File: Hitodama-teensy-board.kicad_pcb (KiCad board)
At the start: 2 copper layers, 119 x 174 mm, 16 parts, among them U4 Teensy3.6

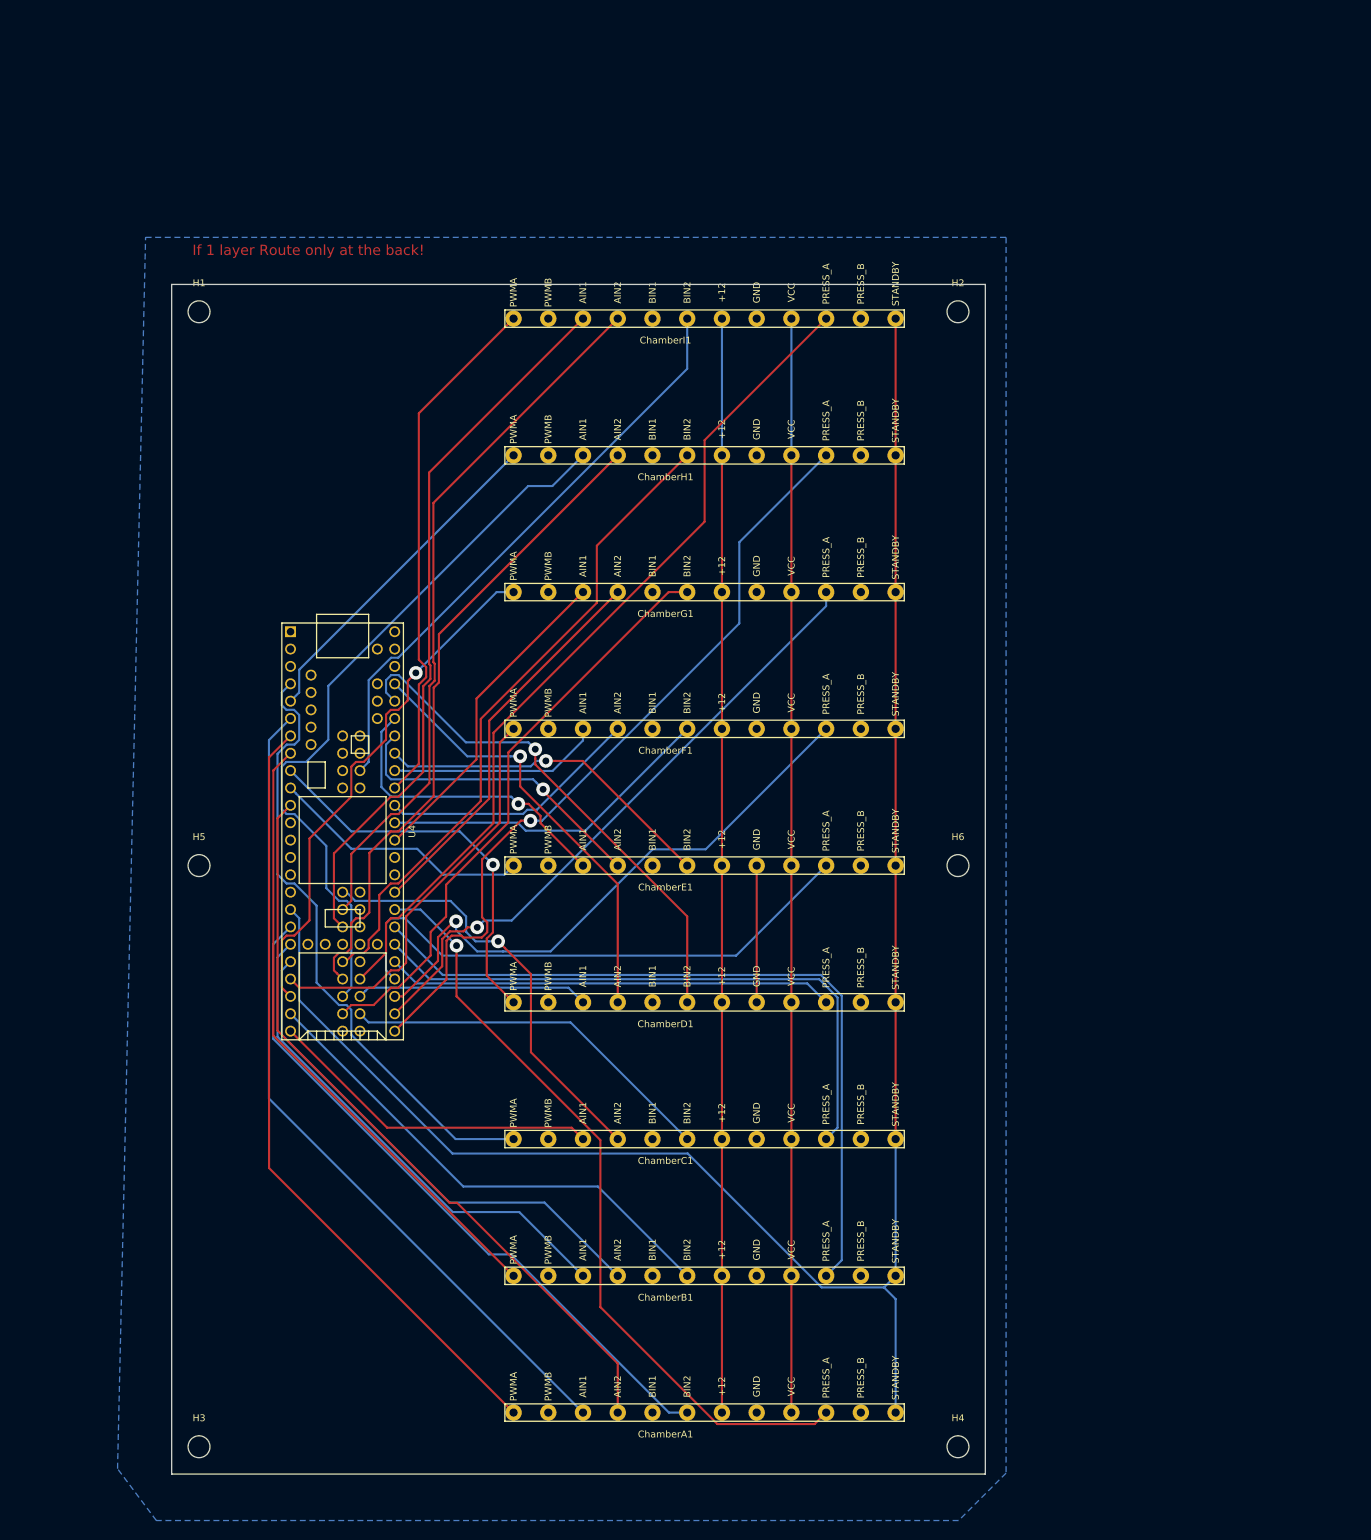
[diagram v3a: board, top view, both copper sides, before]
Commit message: schematic add SPI ports & 12 v power connector
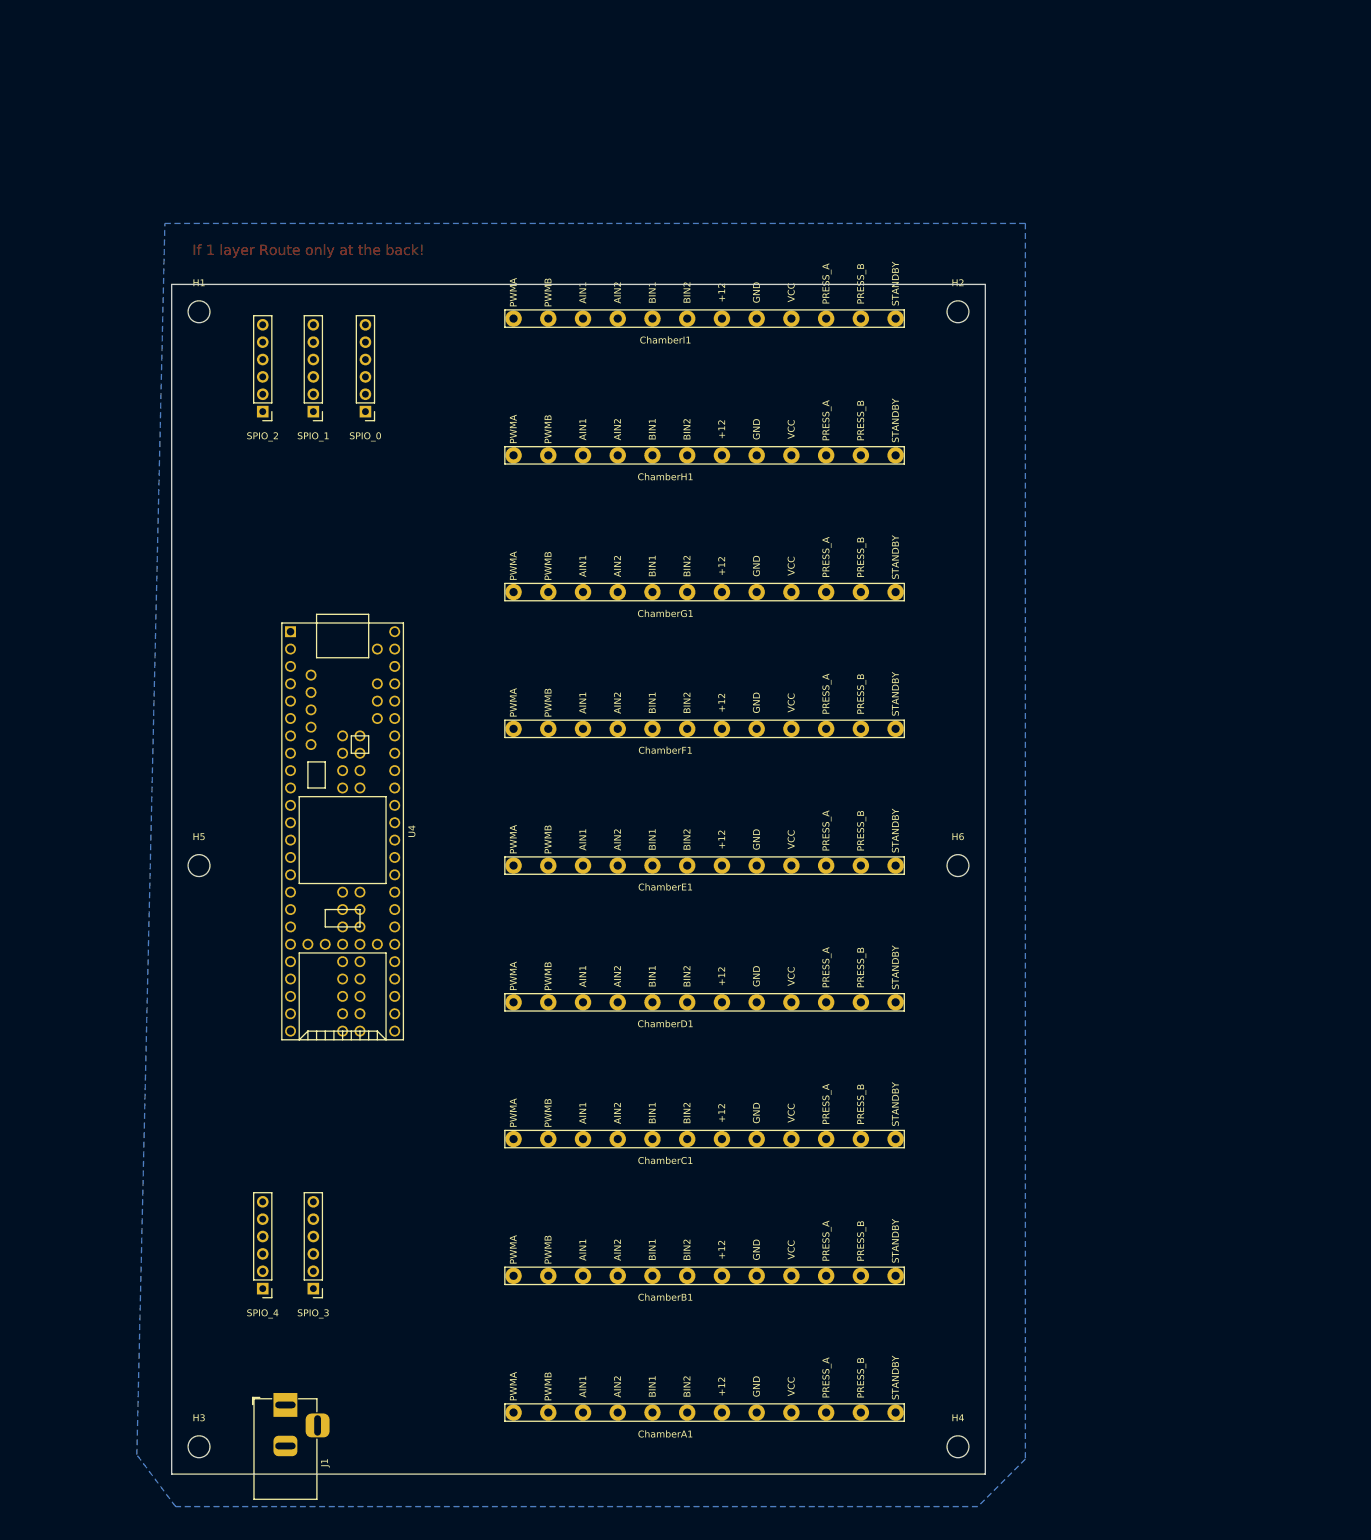
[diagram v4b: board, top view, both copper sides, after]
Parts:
- added J1: Jack-DC, Connector_BarrelJack:BarrelJack_Horizontal, F.Cu at (26.6, 173.9)
- added SPIO_0: Conn_01x06_Female, Connector_PinHeader_2.54mm:PinHeader_1x06_P2.54mm_Vertical, F.Cu at (38.3, 28.6)
- added SPIO_1: Conn_01x06_Female, Connector_PinHeader_2.54mm:PinHeader_1x06_P2.54mm_Vertical, F.Cu at (30.7, 28.6)
- added SPIO_2: Conn_01x06_Female, Connector_PinHeader_2.54mm:PinHeader_1x06_P2.54mm_Vertical, F.Cu at (23.3, 28.6)
- added SPIO_3: Conn_01x06_Female, Connector_PinHeader_2.54mm:PinHeader_1x06_P2.54mm_Vertical, F.Cu at (30.7, 156.9)
- added SPIO_4: Conn_01x06_Female, Connector_PinHeader_2.54mm:PinHeader_1x06_P2.54mm_Vertical, F.Cu at (23.3, 156.9)
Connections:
- U4 pad 80: /D51 -> /SPI0.CS4
- U4 pad 81: /D52 -> /SPI0.CS3
- U4 pad 82: /D53 -> /SPI0.CS2
- U4 pad 83: /D54 -> /SPI0.CS1
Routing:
- net /All.Stby: track 278.1 -> 0.00 mm
- net VCC: track 160.0 -> 0.00 mm
- net +12V: track 160.0 -> 0.00 mm
- net /ChamberI.ADC: track 125.4 -> 0.00 mm
- net /ChamberA.D1: track 121.8 -> 0.00 mm
- net /ChamberH.ADC: track 115.8 -> 0.00 mm, vias 1 -> 0
- net /ChamberA.PWM: track 115.1 -> 0.00 mm
- net /ChamberA.ADC: track 113.6 -> 0.00 mm, vias 1 -> 0
- net /ChamberB.ADC: track 111.5 -> 0.00 mm
- net /ChamberA.D2: track 110.8 -> 0.00 mm
- net /ChamberH.D1: track 107.2 -> 0.00 mm
- net /ChamberI.D1: track 105.4 -> 0.00 mm
- net /ChamberI.D2: track 103.9 -> 0.00 mm
- net /ChamberA.D3: track 100.6 -> 0.00 mm
- net /ChamberH.D3: track 96.7 -> 0.00 mm
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
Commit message: route & DRC teensy board
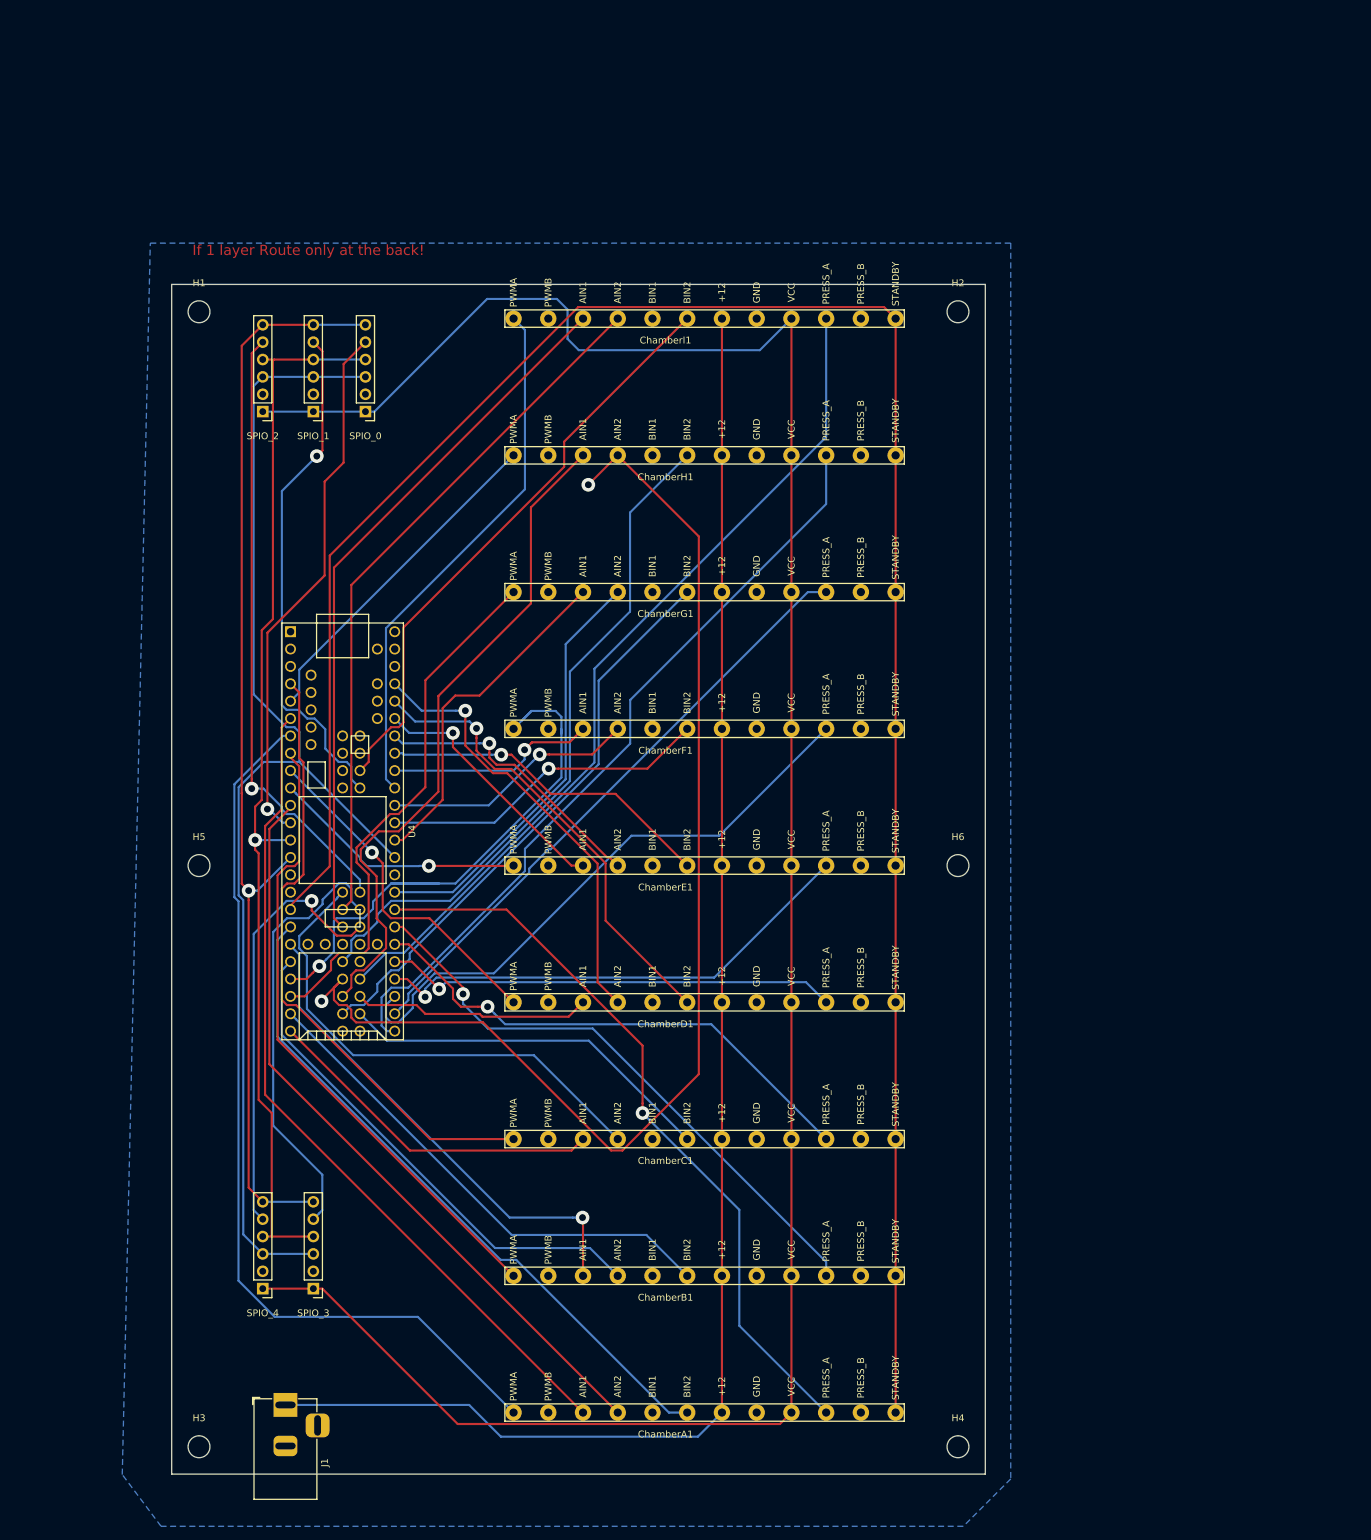
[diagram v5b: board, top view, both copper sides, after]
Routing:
- net VCC: track 0.00 -> 337.9 mm
- net /All.Stby: track 0.00 -> 312.7 mm
- net +12V: track 0.00 -> 227.2 mm
- net /SPI0.SCK: track 0.00 -> 182.6 mm
- net /ChamberH.D2: track 0.00 -> 177.4 mm, vias 0 -> 2
- net /SPI0.MISO: track 0.00 -> 161.4 mm, vias 0 -> 1
- net /SPI0.MOSI: track 0.00 -> 157.9 mm, vias 0 -> 1
- net /ChamberA.PWM: track 0.00 -> 132.2 mm
- net /ChamberI.ADC: track 0.00 -> 126.4 mm
- net /ChamberA.D1: track 0.00 -> 122.3 mm
- net /ChamberH.ADC: track 0.00 -> 114.1 mm
- net /ChamberA.D2: track 0.00 -> 111.2 mm
- net /ChamberA.ADC: track 0.00 -> 109.3 mm, vias 0 -> 1
- net /ChamberI.D1: track 0.00 -> 104.6 mm
- net /ChamberI.D2: track 0.00 -> 103.1 mm
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
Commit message: separated the teensy board into four modules, so that it fits in smaller PCB's. Improved the chamber board, and added rules so that auto-router can figure out the optimal 1 layer+jumpers route
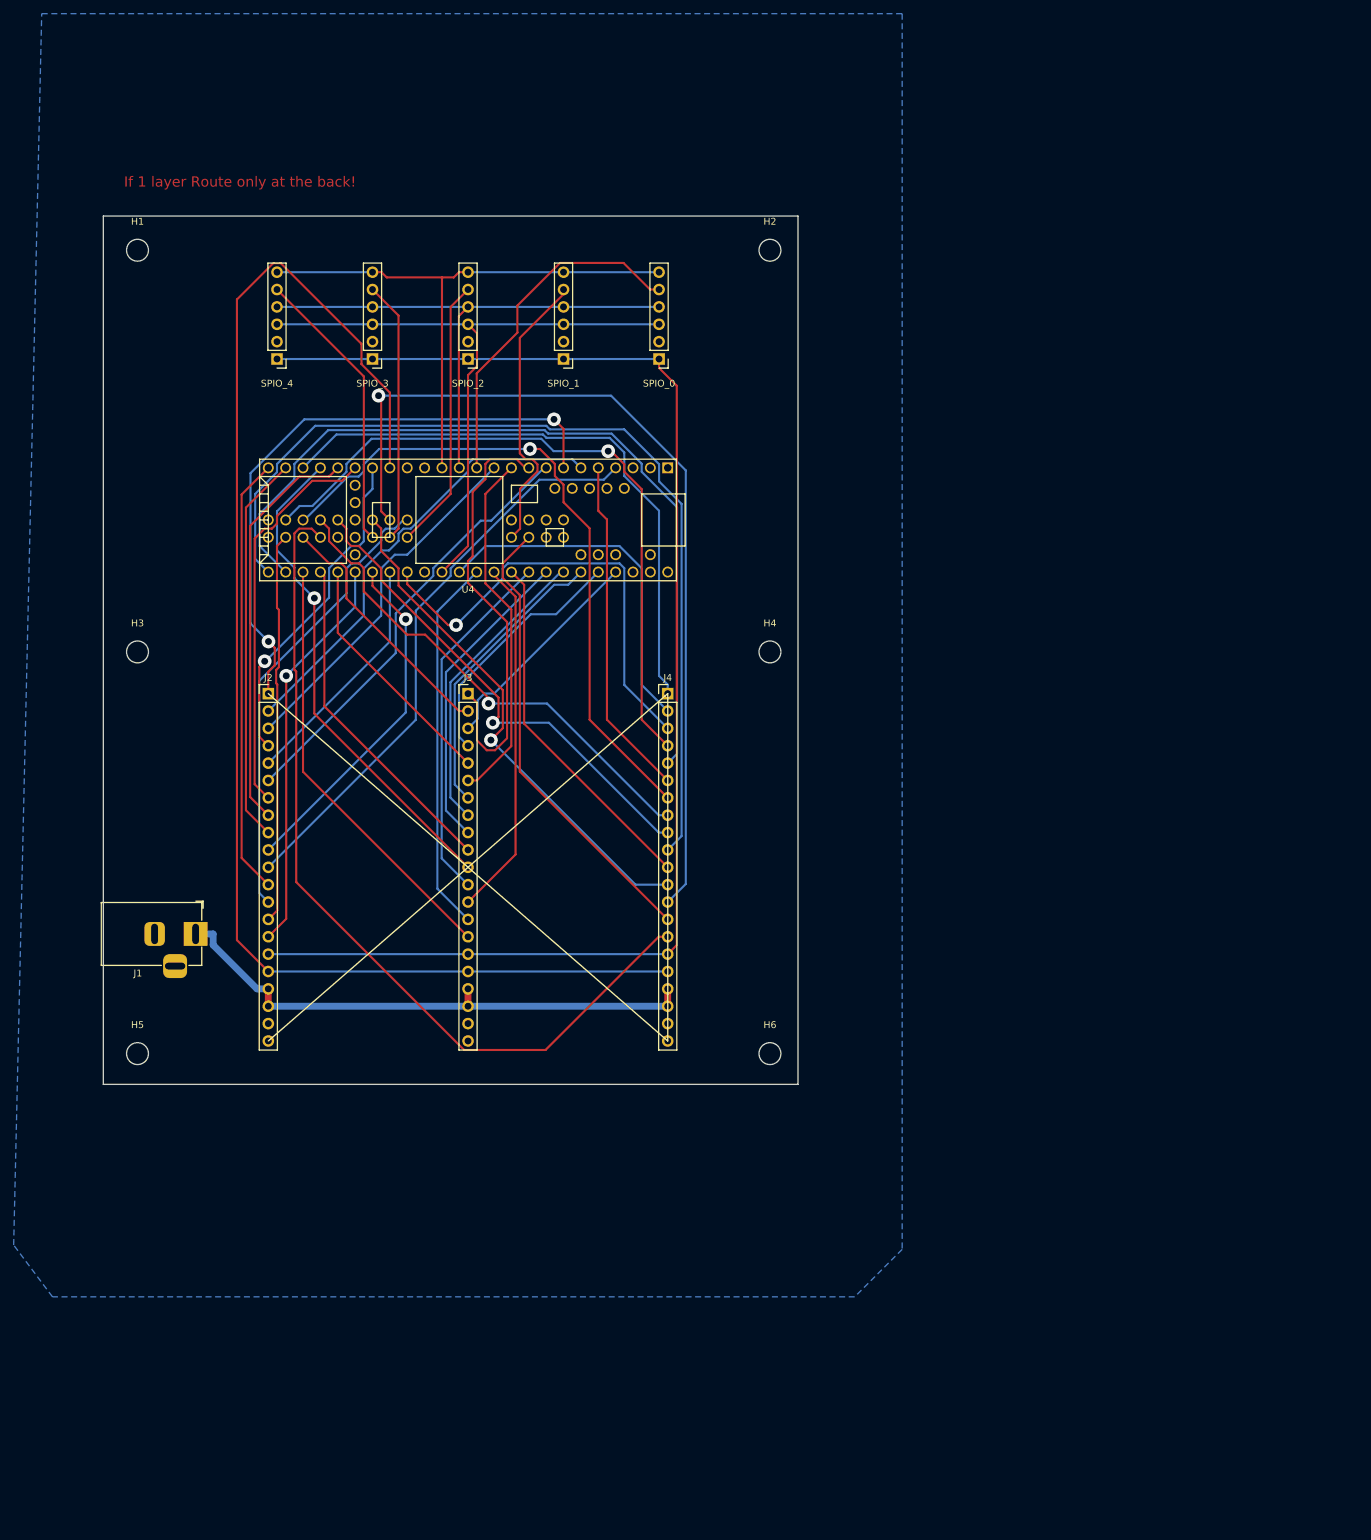
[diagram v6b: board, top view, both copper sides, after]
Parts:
- removed ChamberA1, ChamberB1, ChamberC1, ChamberD1, ChamberE1, ChamberF1, ChamberG1, ChamberH1, ChamberI1: ChamberBoard_Holder, chamber_board_holder:chamber_board_holder
- added J2: Conn_01x21_Female, Connector_PinHeader_2.54mm:PinHeader_1x21_P2.54mm_Vertical, F.Cu at (24.1, 69.8)
- added J3: Conn_01x21_Female, Connector_PinHeader_2.54mm:PinHeader_1x21_P2.54mm_Vertical, F.Cu at (53.3, 69.8)
- added J4: Conn_01x21_Female, Connector_PinHeader_2.54mm:PinHeader_1x21_P2.54mm_Vertical, F.Cu at (82.5, 69.8)
- moved SPIO_3 136.2 mm to (39.4, 20.9)
- moved SPIO_4 136.0 mm to (25.4, 20.9)
- moved H4 119.5 mm to (97.5, 63.8)
- moved H3 116.6 mm to (5.00, 63.8)
- moved J1 70.1 mm to (13.5, 105.0), turned to 0 degrees
- moved U4 49.1 mm to (53.3, 44.5), turned to 180 degrees
- moved SPIO_0 43.6 mm to (81.3, 20.9)
- moved H6 38.9 mm to (97.5, 122.5)
- moved SPIO_1 37.4 mm to (67.3, 20.9)
- moved SPIO_2 31.0 mm to (53.3, 20.9)
- moved H2 28.9 mm to (97.5, 5.00)
- moved H5 28.9 mm to (5.00, 122.5)
- moved H1 12.7 mm to (5.00, 5.00)
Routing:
- net +12V: track 227.2 -> 80.9 mm
- net VCC: track 337.9 -> 203.0 mm
- net /All.Stby: track 312.7 -> 203.8 mm
- net /ChamberH.D2: track 177.4 -> 72.2 mm, vias 2 -> 1
- net /SPI0.SCK: track 182.6 -> 94.8 mm
- net /SPI0.MOSI: track 157.9 -> 80.0 mm, vias 1 -> 0
- net /SPI0.MISO: track 161.4 -> 84.4 mm, vias 1 -> 0
- net /ChamberA.ADC: track 109.3 -> 35.3 mm, vias 1 -> 0
- net /ChamberA.D2: track 111.2 -> 52.8 mm
- net /ChamberA.D1: track 122.3 -> 66.8 mm
- net /ChamberA.D3: track 99.5 -> 48.8 mm, vias 0 -> 1
- net /SPI0.CS2: track 89.3 -> 39.9 mm, vias 1 -> 0
- net /ChamberA.PWM: track 132.2 -> 89.4 mm, vias 0 -> 2
- net /ChamberB.ADC: track 86.8 -> 51.0 mm
- net /SPI0.CS1: track 75.3 -> 42.1 mm, vias 1 -> 0
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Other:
- board size 119 x 174 mm -> 101.6 x 127 mm
- net class Power added: clearance 0.31, trace_width 1, via_dia 2, via_drill 1

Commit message: teensy board change 21 pins headers into 20 pins headers.
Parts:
- J2, J3, J4: value Conn_01x21_Female -> Conn_01x20_Female; footprint Connector_PinHeader_2.54mm:PinHeader_1x21_P2.54mm_Vertical -> Connector_PinHeader_2.54mm:PinHeader_1x20_P2.54mm_Vertical
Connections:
- J2 pad 19: +12V -> GND
- J2 pad 20: GND -> Net-(J2-Pad20)
- J3 pad 19: +12V -> GND
- J3 pad 20: GND -> Net-(J3-Pad20)
- J4 pad 19: +12V -> GND
- J4 pad 20: GND -> Net-(J4-Pad20)
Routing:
- net GND: track 0.00 -> 240.2 mm
- net /ChamberH.ADC: track 137.1 -> 183.0 mm, vias 0 -> 1
- net /ChamberB.PWM: track 63.6 -> 109.1 mm
- net /ChamberC.PWM: track 85.0 -> 119.1 mm
- net /ChamberD.PWM: track 63.8 -> 38.5 mm, vias 0 -> 1
- net /ChamberG.ADC: track 120.9 -> 96.2 mm, vias 0 -> 2
- net /ChamberA.D1: track 66.8 -> 88.1 mm
- net /ChamberA.D2: track 52.8 -> 74.0 mm
- net /ChamberH.D2: track 72.2 -> 91.4 mm, vias 1 -> 0
- net /ChamberH.D3: track 72.6 -> 90.8 mm, vias 1 -> 0
- net /ChamberG.D3: track 100.5 -> 85.6 mm, vias 1 -> 3
- net /ChamberG.D2: track 66.9 -> 52.5 mm, vias 1 -> 2
- net /ChamberG.D1: track 52.0 -> 64.1 mm, vias 0 -> 1
- net /ChamberI.D2: track 132.6 -> 121.5 mm
- net /ChamberI.PWM: track 52.6 -> 63.7 mm
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- removed copper zone on B.Cu, net GND
